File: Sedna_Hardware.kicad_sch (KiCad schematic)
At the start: 50 parts, among them J1 PJ-102A, J10 5-103634-2, J11 2-644488-2, J2 61201021721, J3 Conn_01x14, J4 0878340619, J5 2-644803-3, J6 2-644488-3, J7 1935161, J8 1935161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

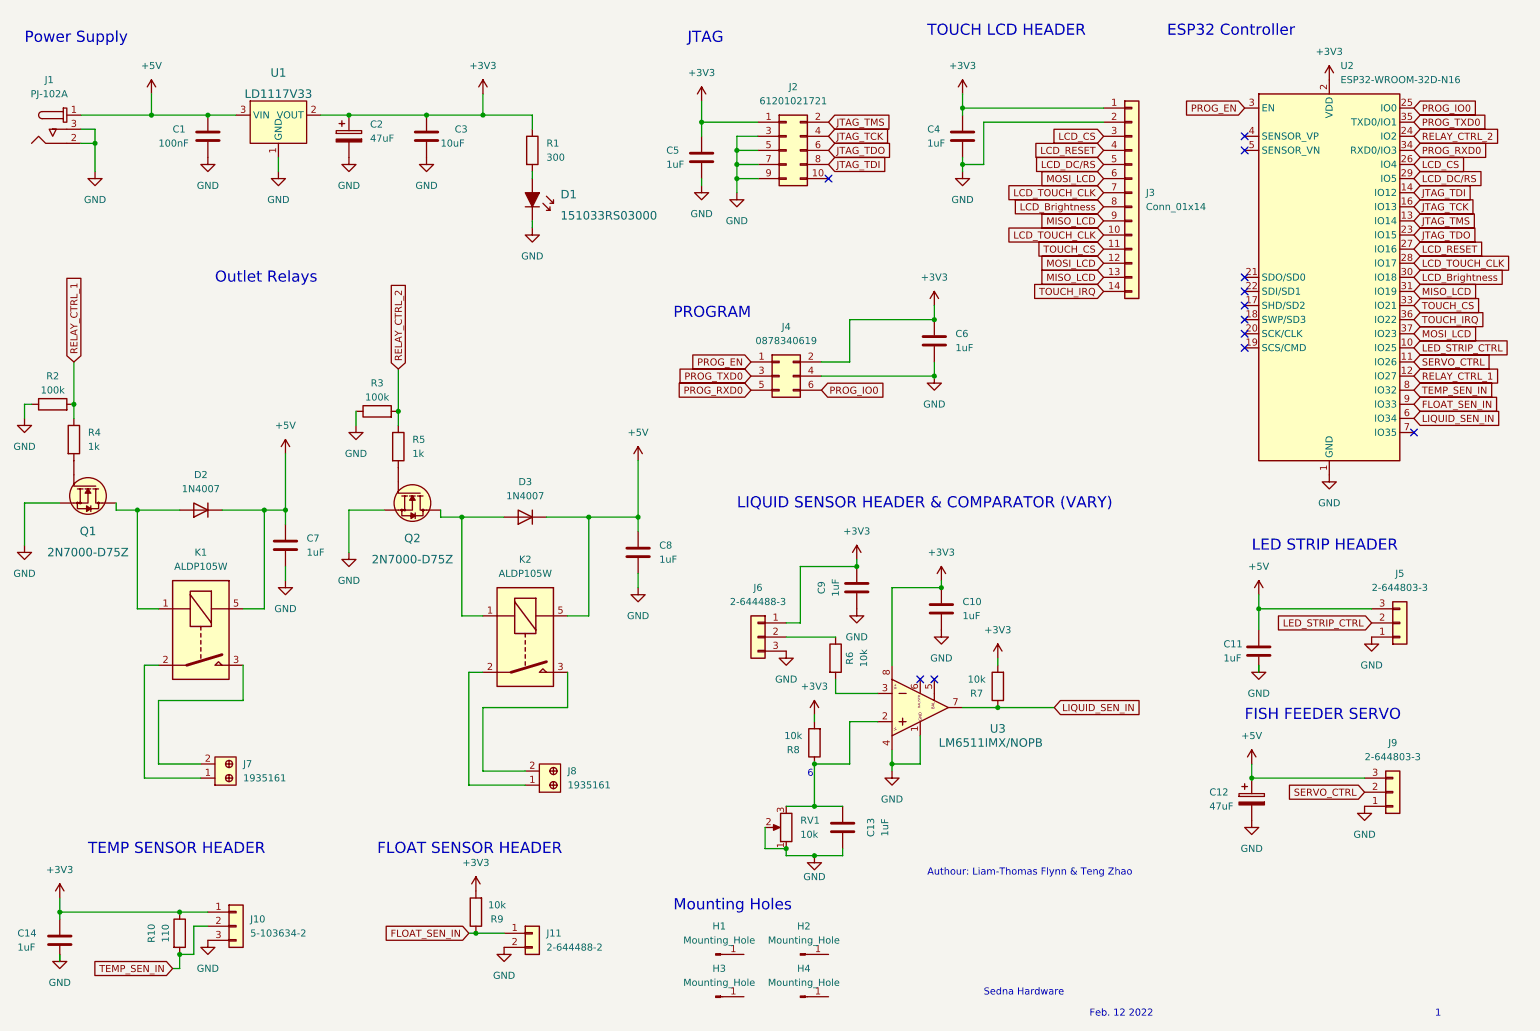
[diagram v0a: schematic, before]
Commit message: finished track layout
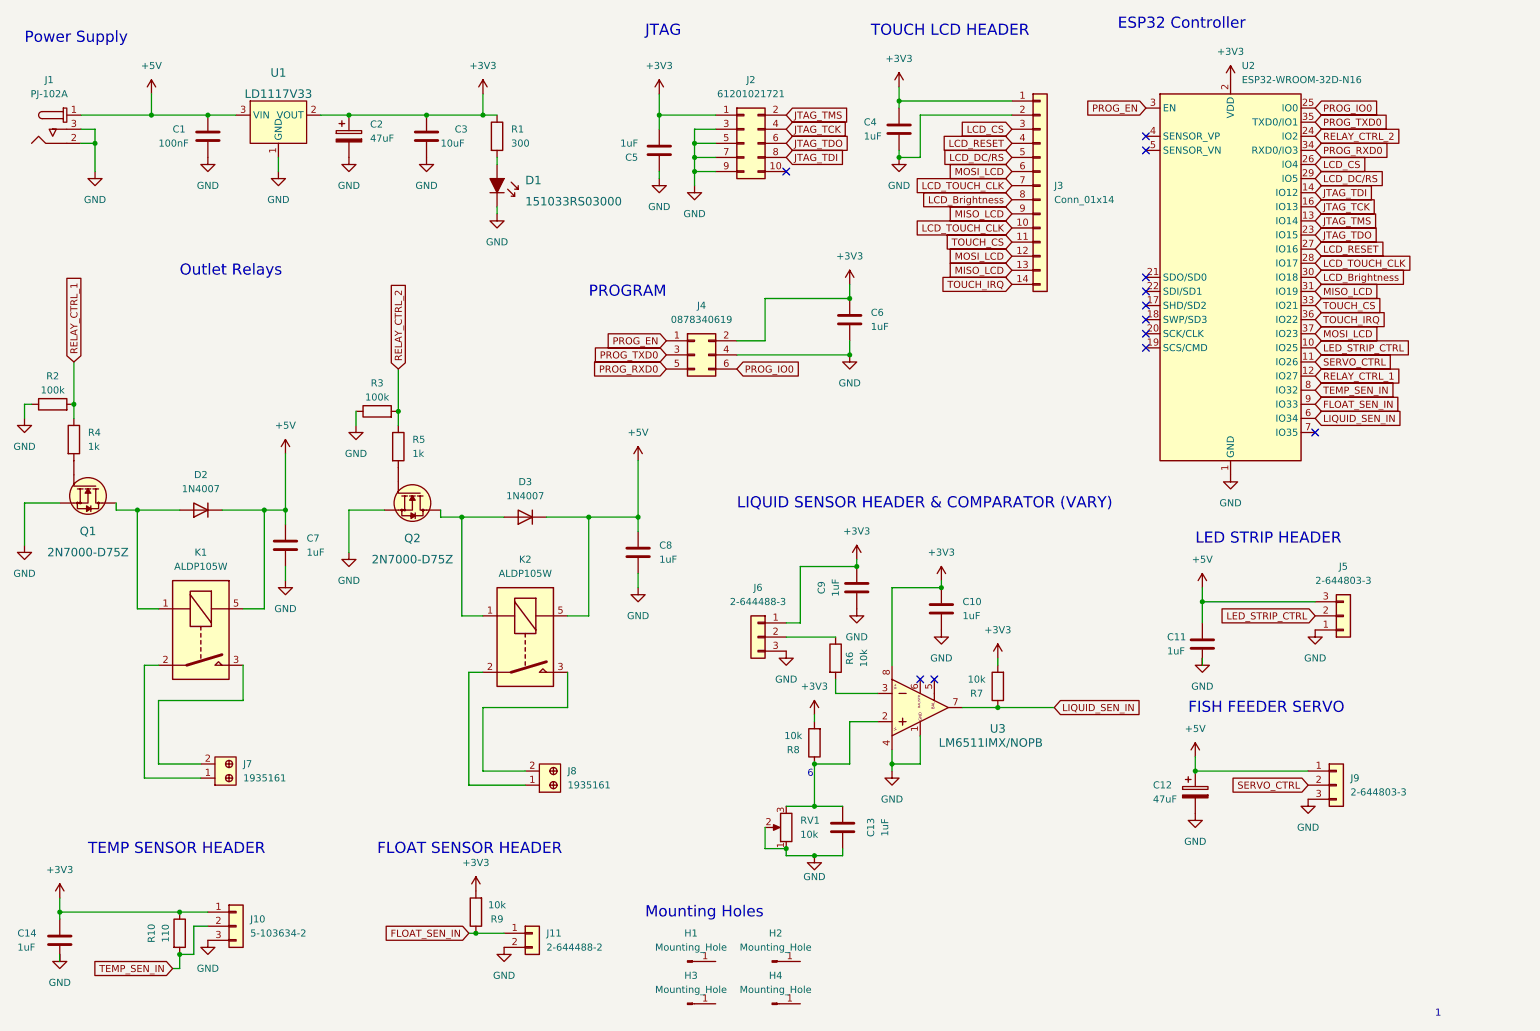
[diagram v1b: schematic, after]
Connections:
- net +3V3: now also C5.2; no longer C5.1
- net +5V: now also J9.1 (Pin_1); no longer J9.3 (Pin_3)
- net GND: now also C5.1, J9.3 (Pin_3); no longer C5.2, J9.1 (Pin_1)
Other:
- note removed: "Authour: Liam-Thomas Flynn & Teng Zhao"
- note removed: "Feb. 12 2022"
- note removed: "Sedna Hardware"
- title: (none) -> Sedna Hardware
- moved on the sheet: C11, C12, C4, C6, D1, H1, H2, H3, H4, J2, J3, J4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

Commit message: modified relay to correct footpring and symbol
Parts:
- removed K1: ALDP105W, Relay_THT:Relay_SPST_TE_PCH-1xxx2M, symbol Relay:TE_PCH-1xxx2M
- added K1: ALDP105W, RELAY_ALDP105W, symbol ALDP105W:ALDP105W
- J3: value Conn_01x14 -> PPTC141LFBN-RC; Category (none) -> Rectangular Connectors - Headers, Receptacles, Female Socke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; DK_Datasheet_Link (none) -> Datasheet; DK_Detail_Page (none) -> https://www.digikey.ca/en/products/detail/sullins-connector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; Digi-Key_PN (none) -> S7012-ND; MPN (none) -> PPTC141LFBN-RC; Manufacturer (none) -> Sullins Connector Solutions; Status (none) -> active
- K2: footprint Relay_THT:Relay_SPST_TE_PCH-1xxx2M -> RELAY_ALDP105W; symbol Relay:TE_PCH-1xxx2M -> ALDP105W:ALDP105W; MF (none) -> Panasonic; PARTREV (none) -> N/A; STANDART (none) -> Manufacturer Recommendations
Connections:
- net +5V: now also K2.1, K1.1; no longer K2.5
- net at D2.2 (A), Q1.3 (D): now also K1.2
- net at J7.1: now also K1.4
- net at J7.2: now also K1.3
- net at D3.2 (A), Q2.3 (D): now also K2.2; no longer K2.1
- net at J8.1: now also K2.4; no longer K2.2
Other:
- moved on the sheet: J8

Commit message: Quick touch ups
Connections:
- no-connect marks 12 -> 16
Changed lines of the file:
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@@
   (no_connect (at 217.17 35.56))
   (no_connect (at 247.65 88.9))
+  (no_connect (at 154.94 191.77))
+  (no_connect (at 154.94 184.15))
+  (no_connect (at 139.7 184.15))
+  (no_connect (at 139.7 191.77))
   (no_connect (at 217.17 60.96))
   (no_connect (at 217.17 66.04))
@@
       (effects (font (size 1.27 1.27)) hide)
     )
-    (property "MF" "Panasonic" (id 12) (at 105.41 127 0)
+    (property "MF" "Panasonic" (id 13) (at 105.41 127 0)
       (effects (font (size 1.27 1.27)) (justify left bottom) hide)
     )
@@
       (effects (font (size 1.27 1.27)) (justify left bottom) hide)
     )
-    (property "PARTREV" "N/A" (id 13) (at 46.99 125.73 0)
+    (property "PARTREV" "N/A" (id 14) (at 46.99 125.73 0)
       (effects (font (size 1.27 1.27)) (justify left bottom) hide)
     )

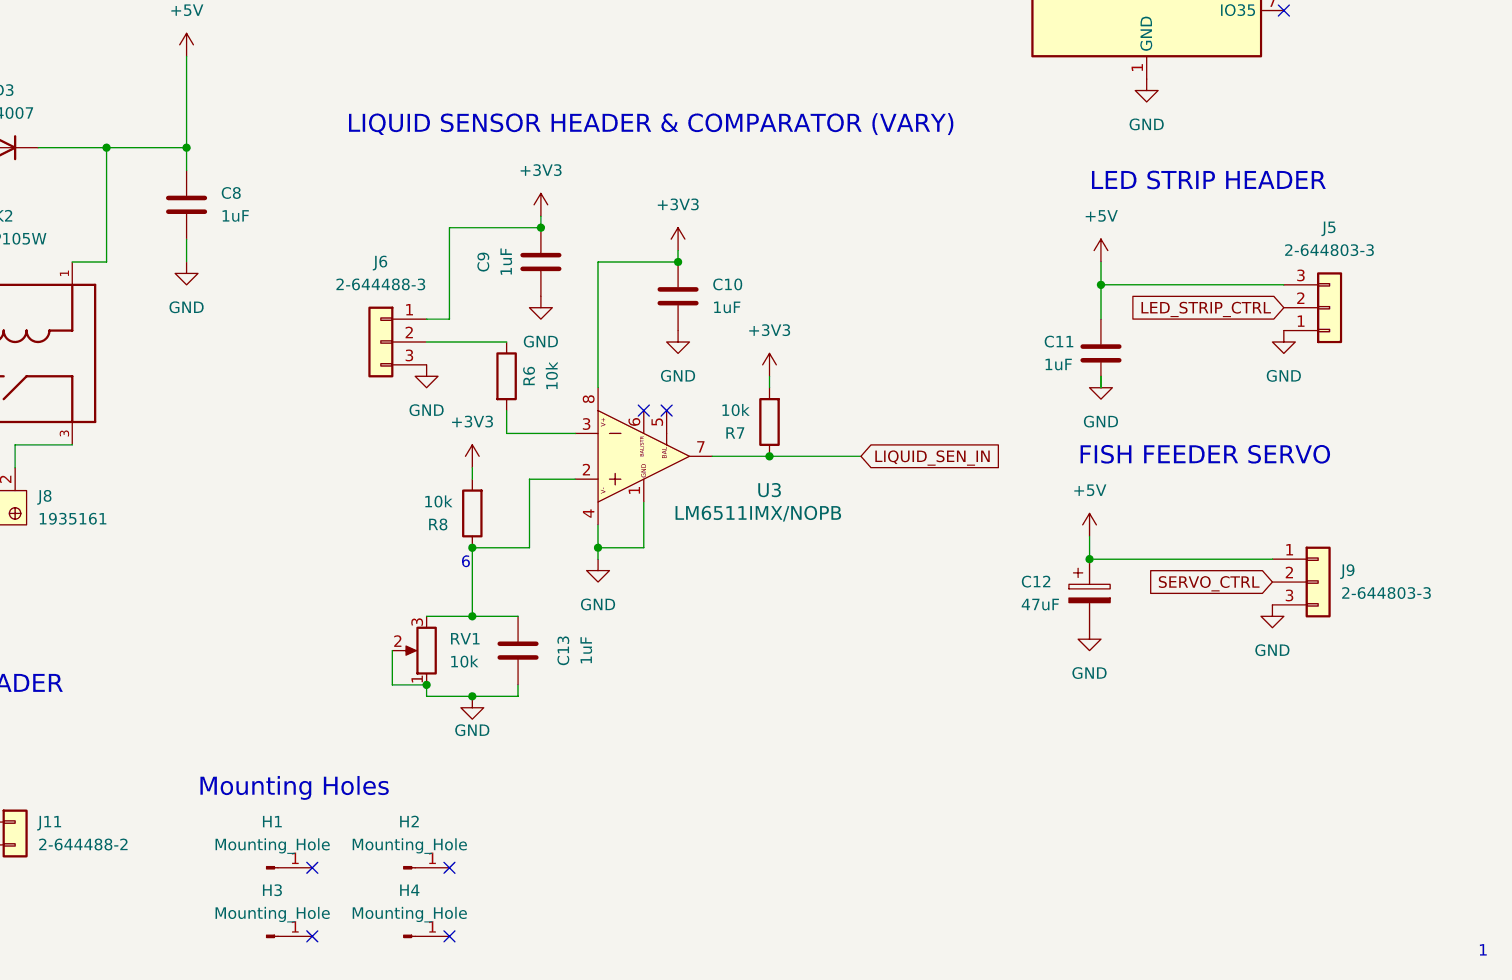
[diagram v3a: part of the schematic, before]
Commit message: added resistor to servo. Placed most of tracks in bottom layer
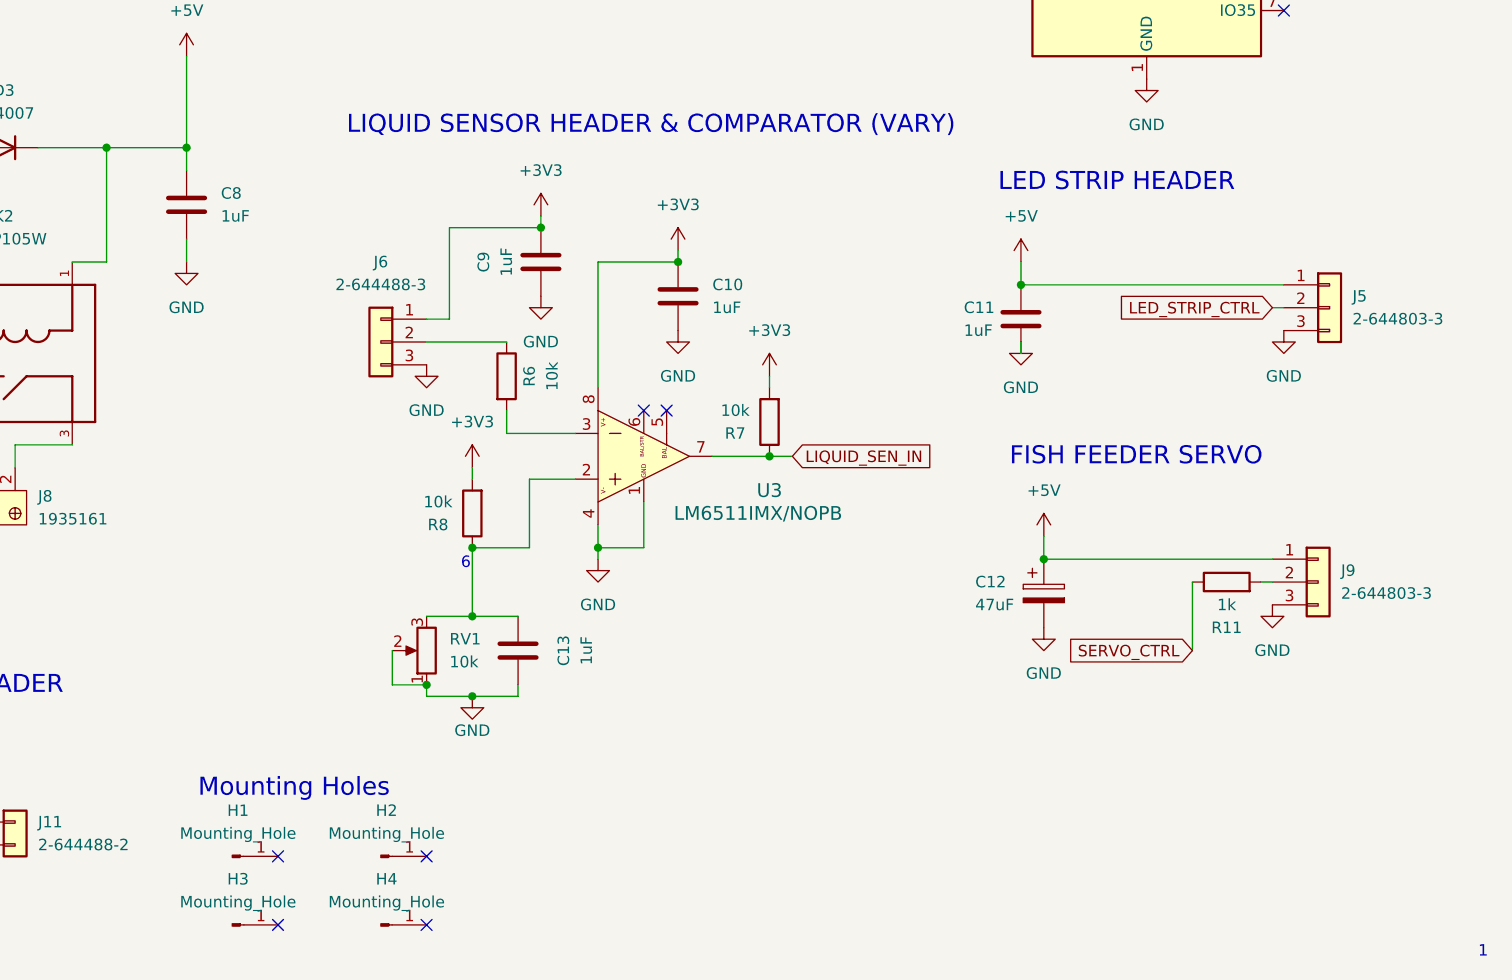
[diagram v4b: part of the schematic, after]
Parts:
- added R11: 1k, Resistor_THT:R_Axial_DIN0204_L3.6mm_D1.6mm_P5.08mm_Horizontal, symbol Device:R
- H1, H2, H3, H4: footprint MountingHole:MountingHole_3.5mm -> MountingHole:MountingHole_3.5mm_Pad
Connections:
- net +5V: now also J5.1 (Pin_1); no longer J5.3 (Pin_3)
- net GND: now also J5.3 (Pin_3); no longer J5.1 (Pin_1)
- net SERVO_CTRL: now also R11.1; no longer J9.2 (Pin_2)
- new net: J9.2 (Pin_2), R11.2
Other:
- moved on the sheet: C11, C12, H2
